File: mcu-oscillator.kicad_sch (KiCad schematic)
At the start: 3 parts, among them Y1 32.768kHz

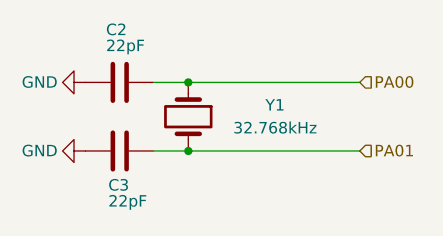
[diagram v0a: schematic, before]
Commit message: Adding symbols information
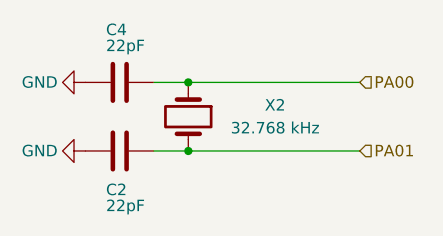
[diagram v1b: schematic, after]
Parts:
- removed C3: 22pF, symbol Device:C
- added C2: 22pF, Capacitor_SMD:C_0603_1608Metric, symbol Device:C
- C4: renamed from C2; footprint (none) -> Capacitor_SMD:C_0603_1608Metric; Mfr (none) -> KEMET; Mfr P/N (none) -> C0603C220K4GAC7867; Supplier_1 (none) -> Digikey; Supplier_1 P/N (none) -> 399-C0603C220K4GAC7867CT-ND; Supplier_1 Price @ Qty (none) -> 0.02630; Supplier_1 Unit Price (none) -> 0.10
- X2: renamed from Y1; value 32.768kHz -> 32.768 kHz; footprint (none) -> Crystal:Crystal_SMD_3215-2Pin_3.2x1.5mm; Mfr (none) -> NDK America, Inc.; Mfr P/N (none) -> STDMUA17-32.768K; Supplier_1 (none) -> Digikey; Supplier_1 P/N (none) -> 644-STDMUA17-32.768KCT-ND; Supplier_1 Price @ Qty (none) -> 0.7610; Supplier_1 Unit Price (none) -> 1.02
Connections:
- net GND: now also C2.2
- net PA01: now also C2.1
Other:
- company: (none) -> catbranchman

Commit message: Spamming 0 ohm resistors
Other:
- title: (none) -> MCU - Oscillator
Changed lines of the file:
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@@
 	(paper "A4")
 	(title_block
+		(title "MCU - Oscillator")
 		(company "catbranchman")
 		(comment 1 "Electrical Engineering Department")
